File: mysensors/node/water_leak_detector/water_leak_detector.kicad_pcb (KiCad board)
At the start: 2 copper layers, 50.6 x 50.6 mm, 6 parts, among them P1 Water Probe, U1 TS881

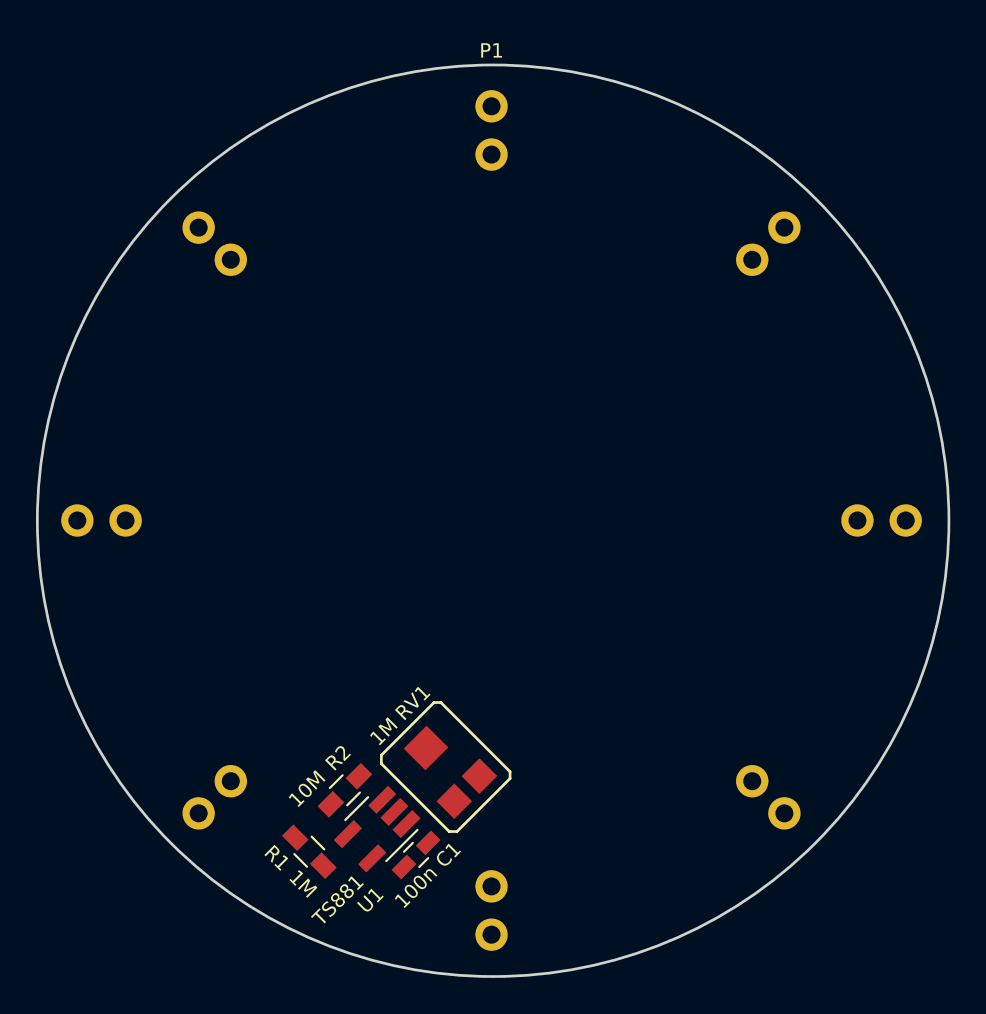
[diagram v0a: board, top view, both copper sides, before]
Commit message: mysensors water leak node - added nrf51822 module
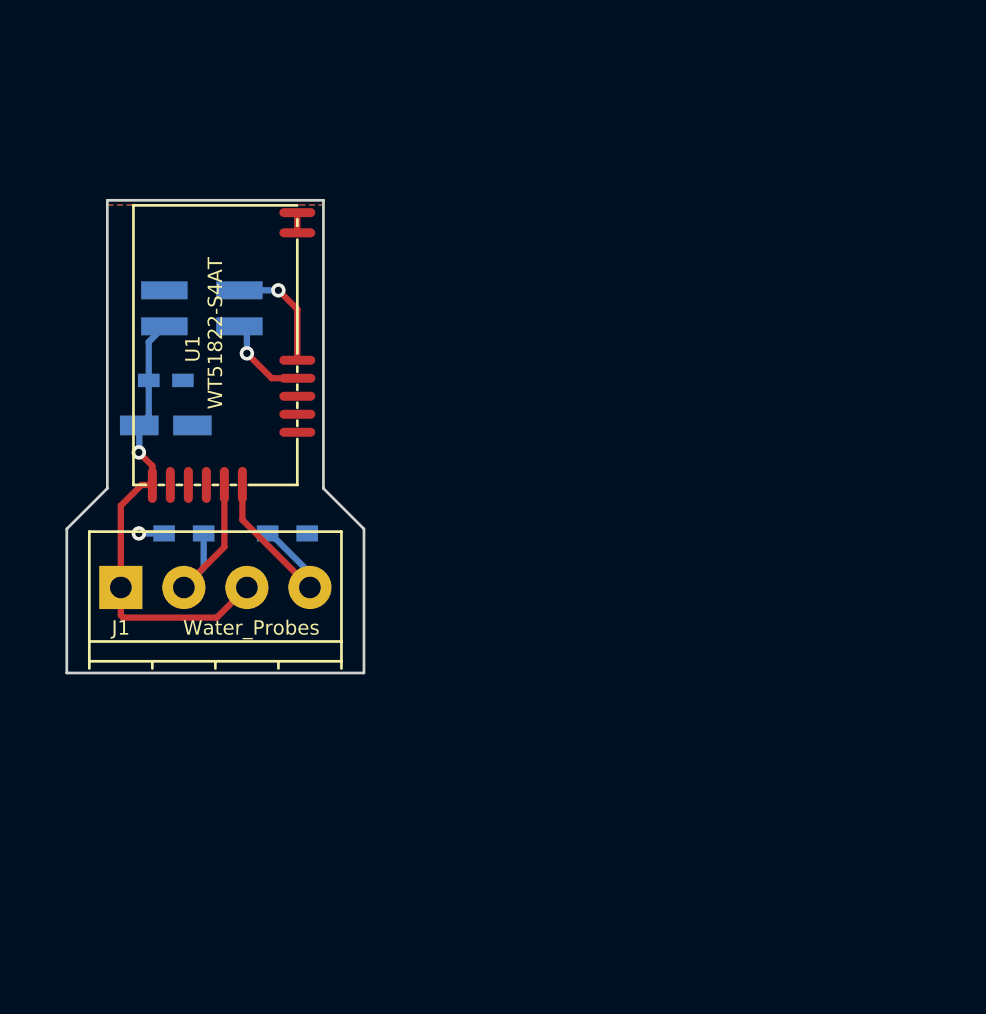
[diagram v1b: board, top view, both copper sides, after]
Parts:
- removed P1: Water Probe, Circular_Water_Sensor_Outline
- removed RV1: 1M, myfootprints:TC-33X-2
- added C2: 100n, Capacitors_SMD:C_0603_HandSoldering, B.Cu at (104.0, 74.5)
- added J1: Water_Probes, Connectors_Terminal_Blocks:TerminalBlock_Pheonix_PT-3.5mm_4pol, F.Cu at (101.5, 86.0)
- added J2: SWD, Pin_Headers:Pin_Header_Straight_2x02_Pitch2.00mm_SMD, B.Cu at (106.0, 70.5)
- C1: value 100n -> 10u; footprint Capacitors_SMD:C_0603_HandSoldering -> Capacitors_Tantalum_SMD:CP_Tantalum_Case-A_EIA-3216-18_Wave; moved to B.Cu
- R1: moved to B.Cu
- R2: value 10M -> 1M; moved to B.Cu
- U1: value TS881 -> WT51822-S4AT; footprint TO_SOT_Packages_SMD:SOT-23-5_HandSoldering -> myfootprints:WT51822-S4AT
- moved U1 29.8 mm to (106.8, 71.1), turned to 0 degrees
- moved C1 27.6 mm to (104.0, 77.0), turned to 0 degrees
- moved R1 17.7 mm to (110.8, 83.0), turned to 0 degrees
- moved R2 16.8 mm to (105.0, 83.0), turned to 180 degrees
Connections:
- C1 pad 1: GND -> +3V3
- C1 pad 2: +3V3 -> GND
- R1 pad 1: Net-(P1-Pad2) -> Net-(J1-Pad4)
- R1 pad 2: Net-(R1-Pad2) -> GND
- R2 pad 1: Net-(R1-Pad2) -> Net-(J1-Pad2)
- U1 pad 1: Net-(U1-Pad1) -> +3V3
- U1 pad 4: Net-(R1-Pad2) -> Net-(U1-Pad4)
- U1 pad 5: +3V3 -> Net-(J1-Pad2)
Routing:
- net +3V3: track 0.00 -> 25.8 mm, vias 0 -> 1
- net Net-(J1-Pad4): track 0.00 -> 11.3 mm
- net Net-(J1-Pad2): track 0.00 -> 10.1 mm
- net /SWDIO: track 0.00 -> 6.48 mm, vias 0 -> 1
- net /SWCLK: track 0.00 -> 5.04 mm, vias 0 -> 1
- net GND: track 0.00 -> 2.53 mm, vias 0 -> 1
- added copper zone on B.Cu, net GND
- added copper zone on F.Cu, net GND
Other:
- board size 50.6 x 50.6 mm -> 16.5 x 26.2 mm
